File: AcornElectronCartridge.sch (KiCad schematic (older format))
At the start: 4 parts, among them U1 74HC00, U2 SST39SF010

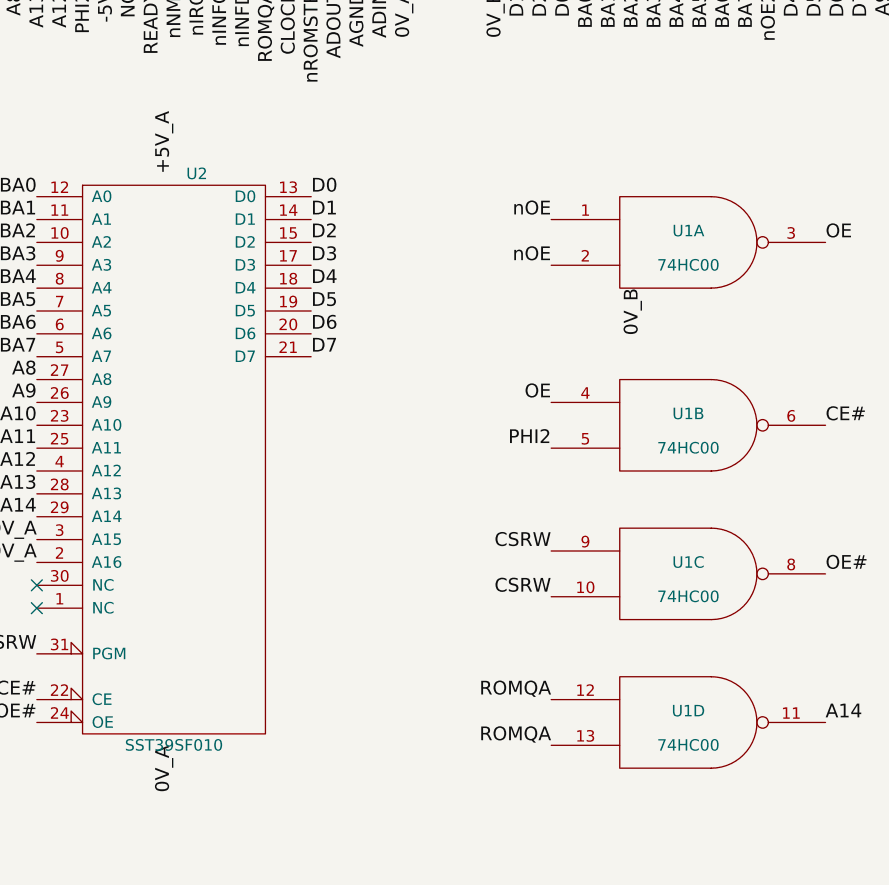
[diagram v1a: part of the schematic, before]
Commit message: Renamed components. Tidied up a little.
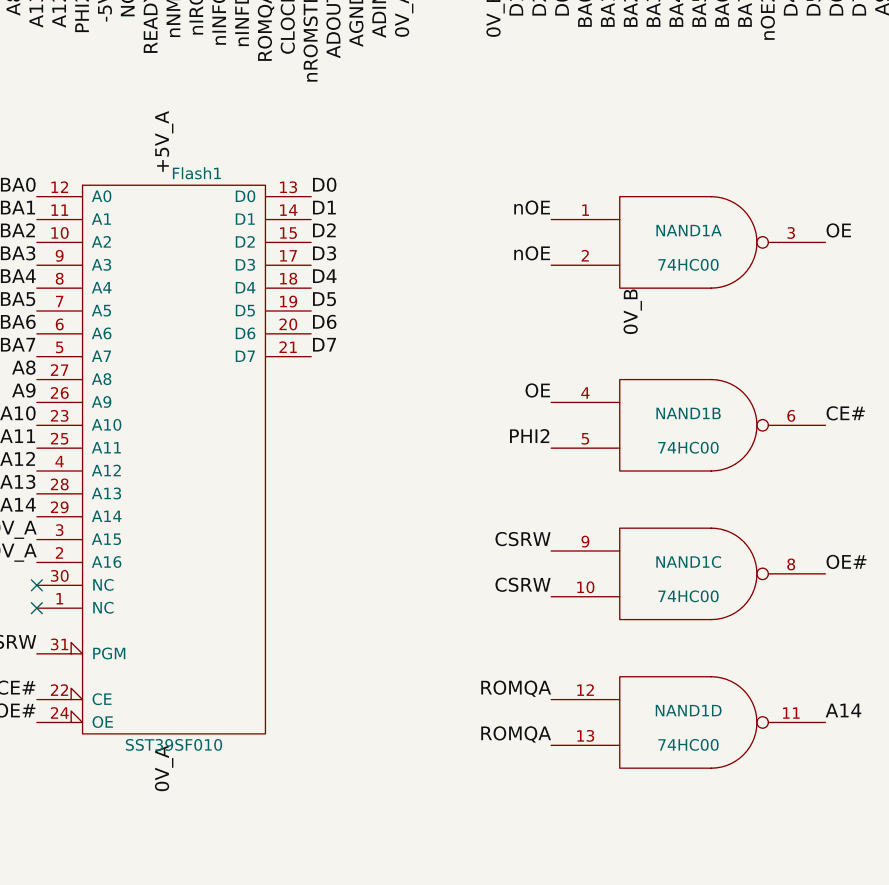
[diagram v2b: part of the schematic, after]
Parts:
- renumbered U2 to Flash1, U1 to NAND1
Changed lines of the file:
@@
 NC
 $Comp
-L 74HC00 U1
+L 74HC00 NAND1
 U 1 1 59D29643
 P 5000 2800
-F 0 "U1" H 5000 2850 50  0000 C CNN
+F 0 "NAND1" H 5000 2850 50  0000 C CNN
 F 1 "74HC00" H 5000 2700 50  0000 C CNN
 F 2 "Housings_DIP:DIP-14_W7.62mm" H 5000 2800 50  0001 C CNN
@@
 $EndComp
 $Comp
-L 74HC00 U1
+L 74HC00 NAND1
 U 2 1 59D29688
 P 5000 3600
-F 0 "U1" H 5000 3650 50  0000 C CNN
+F 0 "NAND1" H 5000 3650 50  0000 C CNN
 F 1 "74HC00" H 5000 3500 50  0000 C CNN
 F 2 "Housings_DIP:DIP-14_W7.62mm" H 5000 3600 50  0001 C CNN
@@
 $EndComp
 $Comp
-L 74HC00 U1
+L 74HC00 NAND1
 U 3 1 59D296BF
 P 5000 4250
-F 0 "U1" H 5000 4300 50  0000 C CNN
+F 0 "NAND1" H 5000 4300 50  0000 C CNN
 F 1 "74HC00" H 5000 4150 50  0000 C CNN
 F 2 "Housings_DIP:DIP-14_W7.62mm" H 5000 4250 50  0001 C CNN
@@
 $EndComp
 $Comp
-L 74HC00 U1
+L 74HC00 NAND1
 U 4 1 59D296F2
 P 5000 4900
-F 0 "U1" H 5000 4950 50  0000 C CNN
+F 0 "NAND1" H 5000 4950 50  0000 C CNN
 F 1 "74HC00" H 5000 4800 50  0000 C CNN
 F 2 "Housings_DIP:DIP-14_W7.62mm" H 5000 4900 50  0001 C CNN
@@
 A14
 $Comp
-L SST39SF010 U2
+L SST39SF010 Flash1
 U 1 1 59D2A464
 P 2750 3800
-F 0 "U2" H 2850 5100 50  0000 C CNN
+F 0 "Flash1" H 2850 5100 50  0000 C CNN
 F 1 "SST39SF010" H 2750 2600 50  0000 C CNN
 F 2 "Housings_DIP:DIP-32_W15.24mm" H 2750 4100 50  0001 C CNN

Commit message: More minor improvements.
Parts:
- added 0V1, 5V1, PADS1: CONN_01X02, Pin_Headers:Pin_Header_Straight_1x02_Pitch2.54mm, symbol CONN_01X02
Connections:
- net +5V_B is gone; now on net VCC: CONN2.1 (+5V)
- net GND: now also 0V1.1 (P1), 0V1.2 (P2); no longer Flash1.2 (A16), Flash1.3 (A15)
- net VCC: now also 5V1.1 (P1), 5V1.2 (P2)
- new net PAD0: Flash1.2 (A16), PADS1.1 (P1)
- new net PAD1: Flash1.3 (A15), PADS1.2 (P2)
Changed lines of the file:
@@
 Text Label 2150 4000 2    60   ~ 0
 A14
-Text Label 2150 4100 2    60   ~ 0
-0V_A
-Text Label 2150 4200 2    60   ~ 0
-0V_A
 Text Label 2750 2500 1    60   ~ 0
 +5V_A
@@
 Text Label 2150 4600 2    60   ~ 0
 CSRW
+$Comp
+L CONN_01X02 PADS1
+U 1 1 59D3C5F5
+P 4800 5550
+F 0 "PADS1" H 4800 5700 50  0000 C CNN
+F 1 "CONN_01X02" V 4900 5550 50  0000 C CNN
+F 2 "Pin_Headers:Pin_Header_Straight_1x02_Pitch2.54mm" H 4800 5550 50  0001 C CNN
+F 3 "" H 4800 5550 50  0000 C CNN
+	1    4800 5550
+	1    0    0    -1
+$EndComp
+Text Label 2150 4100 2    60   ~ 0
+PAD1
+Text Label 2150 4200 2    60   ~ 0
+PAD0
+Text Label 4600 5500 2    60   ~ 0
+PAD0
+Text Label 4600 5600 2    60   ~ 0
+PAD1
+$Comp
+L CONN_01X02 5V1
+U 1 1 59D3E2A3
+P 4800 6100
+F 0 "5V1" H 4800 6250 50  0000 C CNN
+F 1 "CONN_01X02" V 4900 6100 50  0000 C CNN
+F 2 "Pin_Headers:Pin_Header_Straight_1x02_Pitch2.54mm" H 4800 6100 50  0001 C CNN
+F 3 "" H 4800 6100 50  0000 C CNN
+	1    4800 6100
+	1    0    0    -1
+$EndComp
+$Comp
+L CONN_01X02 0V1
+U 1 1 59D3E2FF
+P 4800 6700
+F 0 "0V1" H 4800 6850 50  0000 C CNN
+F 1 "CONN_01X02" V 4900 6700 50  0000 C CNN
+F 2 "Pin_Headers:Pin_Header_Straight_1x02_Pitch2.54mm" H 4800 6700 50  0001 C CNN
+F 3 "" H 4800 6700 50  0000 C CNN
+	1    4800 6700
+	1    0    0    -1
+$EndComp
+Text Label 4600 6050 2    60   ~ 0
++5V_A
+Text Label 4600 6150 2    60   ~ 0
++5V_A
+Text Label 4600 6650 2    60   ~ 0
+0V_A
+Text Label 4600 6750 2    60   ~ 0
+0V_A
+Text Label 4800 2600 1    60   ~ 0
++5V_B
 $EndSCHEMATC

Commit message: Removed the pads and added flip-flops to support the use of the FC73 paging register for software-enabled bank selection.
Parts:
- removed 0V1, 5V1, PADS1: CONN_01X02, Pin_Headers:Pin_Header_Straight_1x02_Pitch2.54mm, symbol CONN_01X02
- added FLIP1: 74LS174, Housings_DIP:DIP-16_W7.62mm_Socket, symbol 74LS174
- NAND1: footprint Housings_DIP:DIP-14_W7.62mm -> Housings_DIP:DIP-14_W7.62mm_Socket
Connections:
- net D0: now also FLIP1.3 (D0)
- net D1: now also FLIP1.4 (D1)
- net GND: now also FLIP1.8 (GND)
- net VCC: now also FLIP1.16 (VCC)
- net nROMSTB: now also FLIP1.9 (Cp)
- net nRST: now also FLIP1.1 (~Mr)
- net PAD0 renamed A16
- net A16: now also FLIP1.5 (Q1)
- net PAD1 renamed A15
- net A15: now also FLIP1.2 (Q0)
- no-connect marks 3 -> 12
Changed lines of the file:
@@
 encoding utf-8
 Sheet 1 1
-Title "Acorn Electron 32K EEPROM cartridge"
+Title "Acorn Electron 128K banked Flash ROM cartridge"
 Date "2017-10-02"
 Rev ""
@@
 F 0 "NAND1" H 5000 2850 50  0000 C CNN
 F 1 "74HC00" H 5000 2700 50  0000 C CNN
-F 2 "Housings_DIP:DIP-14_W7.62mm" H 5000 2800 50  0001 C CNN
+F 2 "Housings_DIP:DIP-14_W7.62mm_Socket" H 5000 2800 50  0001 C CNN
 F 3 "" H 5000 2800 50  0000 C CNN
 	1    5000 2800
@@
 F 0 "NAND1" H 5000 3650 50  0000 C CNN
 F 1 "74HC00" H 5000 3500 50  0000 C CNN
-F 2 "Housings_DIP:DIP-14_W7.62mm" H 5000 3600 50  0001 C CNN
+F 2 "Housings_DIP:DIP-14_W7.62mm_Socket" H 5000 3600 50  0001 C CNN
 F 3 "" H 5000 3600 50  0000 C CNN
 	2    5000 3600
@@
 F 0 "NAND1" H 5000 4300 50  0000 C CNN
 F 1 "74HC00" H 5000 4150 50  0000 C CNN
-F 2 "Housings_DIP:DIP-14_W7.62mm" H 5000 4250 50  0001 C CNN
+F 2 "Housings_DIP:DIP-14_W7.62mm_Socket" H 5000 4250 50  0001 C CNN
 F 3 "" H 5000 4250 50  0000 C CNN
 	3    5000 4250
@@
 F 0 "NAND1" H 5000 4950 50  0000 C CNN
 F 1 "74HC00" H 5000 4800 50  0000 C CNN
-F 2 "Housings_DIP:DIP-14_W7.62mm" H 5000 4900 50  0001 C CNN
+F 2 "Housings_DIP:DIP-14_W7.62mm_Socket" H 5000 4900 50  0001 C CNN
 F 3 "" H 5000 4900 50  0000 C CNN
 	4    5000 4900
@@
 Text Label 2150 4600 2    60   ~ 0
 CSRW
-$Comp
-L CONN_01X02 PADS1
-U 1 1 59D3C5F5
-P 4800 5550
-F 0 "PADS1" H 4800 5700 50  0000 C CNN
-F 1 "CONN_01X02" V 4900 5550 50  0000 C CNN
-F 2 "Pin_Headers:Pin_Header_Straight_1x02_Pitch2.54mm" H 4800 5550 50  0001 C CNN
-F 3 "" H 4800 5550 50  0000 C CNN
-	1    4800 5550
-	1    0    0    -1
-$EndComp
-Text Label 2150 4100 2    60   ~ 0
-PAD1
-Text Label 2150 4200 2    60   ~ 0
-PAD0
-Text Label 4600 5500 2    60   ~ 0
-PAD0
-Text Label 4600 5600 2    60   ~ 0
-PAD1
-$Comp
-L CONN_01X02 5V1
-U 1 1 59D3E2A3
-P 4800 6100
-F 0 "5V1" H 4800 6250 50  0000 C CNN
-F 1 "CONN_01X02" V 4900 6100 50  0000 C CNN
-F 2 "Pin_Headers:Pin_Header_Straight_1x02_Pitch2.54mm" H 4800 6100 50  0001 C CNN
-F 3 "" H 4800 6100 50  0000 C CNN
-	1    4800 6100
-	1    0    0    -1
-$EndComp
-$Comp
-L CONN_01X02 0V1
-U 1 1 59D3E2FF
-P 4800 6700
-F 0 "0V1" H 4800 6850 50  0000 C CNN
-F 1 "CONN_01X02" V 4900 6700 50  0000 C CNN
-F 2 "Pin_Headers:Pin_Header_Straight_1x02_Pitch2.54mm" H 4800 6700 50  0001 C CNN
-F 3 "" H 4800 6700 50  0000 C CNN
-	1    4800 6700
-	1    0    0    -1
-$EndComp
-Text Label 4600 6050 2    60   ~ 0
-+5V_A
-Text Label 4600 6150 2    60   ~ 0
-+5V_A
-Text Label 4600 6650 2    60   ~ 0
-0V_A
-Text Label 4600 6750 2    60   ~ 0
-0V_A
 Text Label 4800 2600 1    60   ~ 0
 +5V_B
+Text Label 7100 3400 2    60   ~ 0
+nRST
+Text Label 7100 3250 2    60   ~ 0
+nROMSTB
+Text Label 7100 2600 2    60   ~ 0
+D0
+Text Label 7100 2700 2    60   ~ 0
+D1
+$Comp
+L 74LS174 FLIP1
+U 1 1 59D8067A
+P 7800 3000
+F 0 "FLIP1" H 7800 3050 50  0000 C CNN
+F 1 "74LS174" H 7800 2850 50  0000 C CNN
+F 2 "Housings_DIP:DIP-16_W7.62mm_Socket" H 7800 3000 50  0001 C CNN
+F 3 "" H 7800 3000 50  0000 C CNN
+	1    7800 3000
+	1    0    0    -1
+$EndComp
+Text Label 7800 2550 1    60   ~ 0
++5V_B
+Text Label 7800 3450 3    60   ~ 0
+0V_B
+Text Label 8500 2600 0    60   ~ 0
+A15
+Text Label 8500 2700 0    60   ~ 0
+A16
+NoConn ~ 8500 2700
+NoConn ~ 8500 2800
+NoConn ~ 8500 2900
+NoConn ~ 8500 3000
+NoConn ~ 8500 3100
+NoConn ~ 7100 3100
+NoConn ~ 7100 3000
+NoConn ~ 7100 2900
+NoConn ~ 7100 2800
+Text Label 2150 4100 2    60   ~ 0
+A15
+Text Label 2150 4200 2    60   ~ 0
+A16
 $EndSCHEMATC

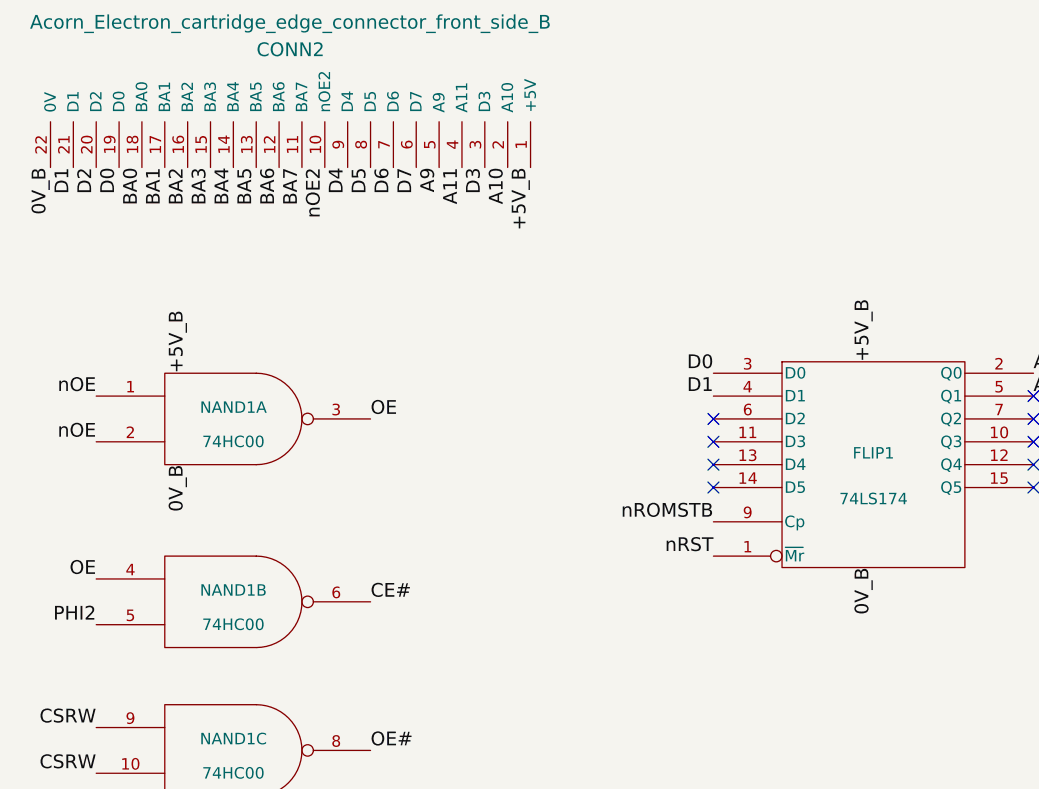
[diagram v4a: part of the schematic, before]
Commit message: Tidied up tracks to leave more space between silkscreen markings and vias. Only used one +5V line and kept the 0V lines separate.
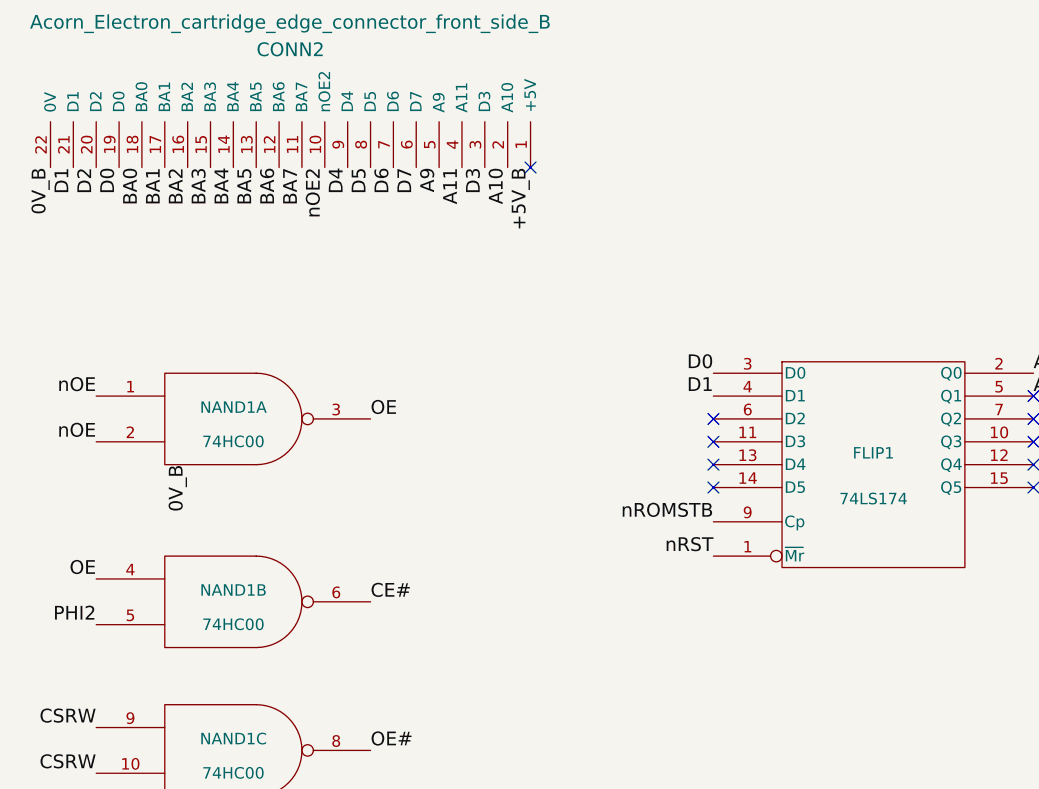
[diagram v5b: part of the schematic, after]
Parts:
- Flash1: footprint Housings_DIP:DIP-32_W15.24mm -> Housings_DIP:DIP-32_W15.24mm_Socket
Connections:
- net VCC: no longer CONN2.1 (+5V)
- new net +5V_B: CONN2.1 (+5V)
- no-connect marks 12 -> 13
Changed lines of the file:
@@
 F 0 "Flash1" H 2850 5100 50  0000 C CNN
 F 1 "SST39SF010" H 2750 2600 50  0000 C CNN
-F 2 "Housings_DIP:DIP-32_W15.24mm" H 2750 4100 50  0001 C CNN
+F 2 "Housings_DIP:DIP-32_W15.24mm_Socket" H 2750 4100 50  0001 C CNN
 F 3 "" H 2750 4100 50  0000 C CNN
 	1    2750 3800
@@
 Text Label 2150 4000 2    60   ~ 0
 A14
-Text Label 2750 2500 1    60   ~ 0
-+5V_A
-Text Label 2750 5000 3    60   ~ 0
-0V_A
 NoConn ~ 2150 4300
 NoConn ~ 2150 4400
 NoConn ~ 5450 7550
-Text Label 4800 3000 3    60   ~ 0
-0V_B
 Text Label 2150 4600 2    60   ~ 0
 CSRW
-Text Label 4800 2600 1    60   ~ 0
-+5V_B
 Text Label 7100 3400 2    60   ~ 0
 nRST
@@
 	1    0    0    -1
 $EndComp
-Text Label 7800 2550 1    60   ~ 0
-+5V_B
-Text Label 7800 3450 3    60   ~ 0
-0V_B
 Text Label 8500 2600 0    60   ~ 0
 A15
@@
 Text Label 2150 4200 2    60   ~ 0
 A16
+NoConn ~ 6300 1700
+Text Label 4800 3000 3    60   ~ 0
+0V_B
+Text Label 2750 5000 3    60   ~ 0
+0V_A
+Text Label 2750 2500 1    60   ~ 0
++5V_A
 $EndSCHEMATC
